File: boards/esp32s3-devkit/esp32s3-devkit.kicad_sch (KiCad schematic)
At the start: 37 parts, among them J1 Conn_01x17_Pin, J2 Conn_01x17_Pin, J3 USB_C_Receptacle_USB2.0_16P, Q1 Q_PMOS_GSD, SW1 ON/OFF, SW2 RESET, SW3 BOOT, U1 TPS630701RNMR, U2 ESP32-S3-WROOM-1, U3 USBLC6-2SC6

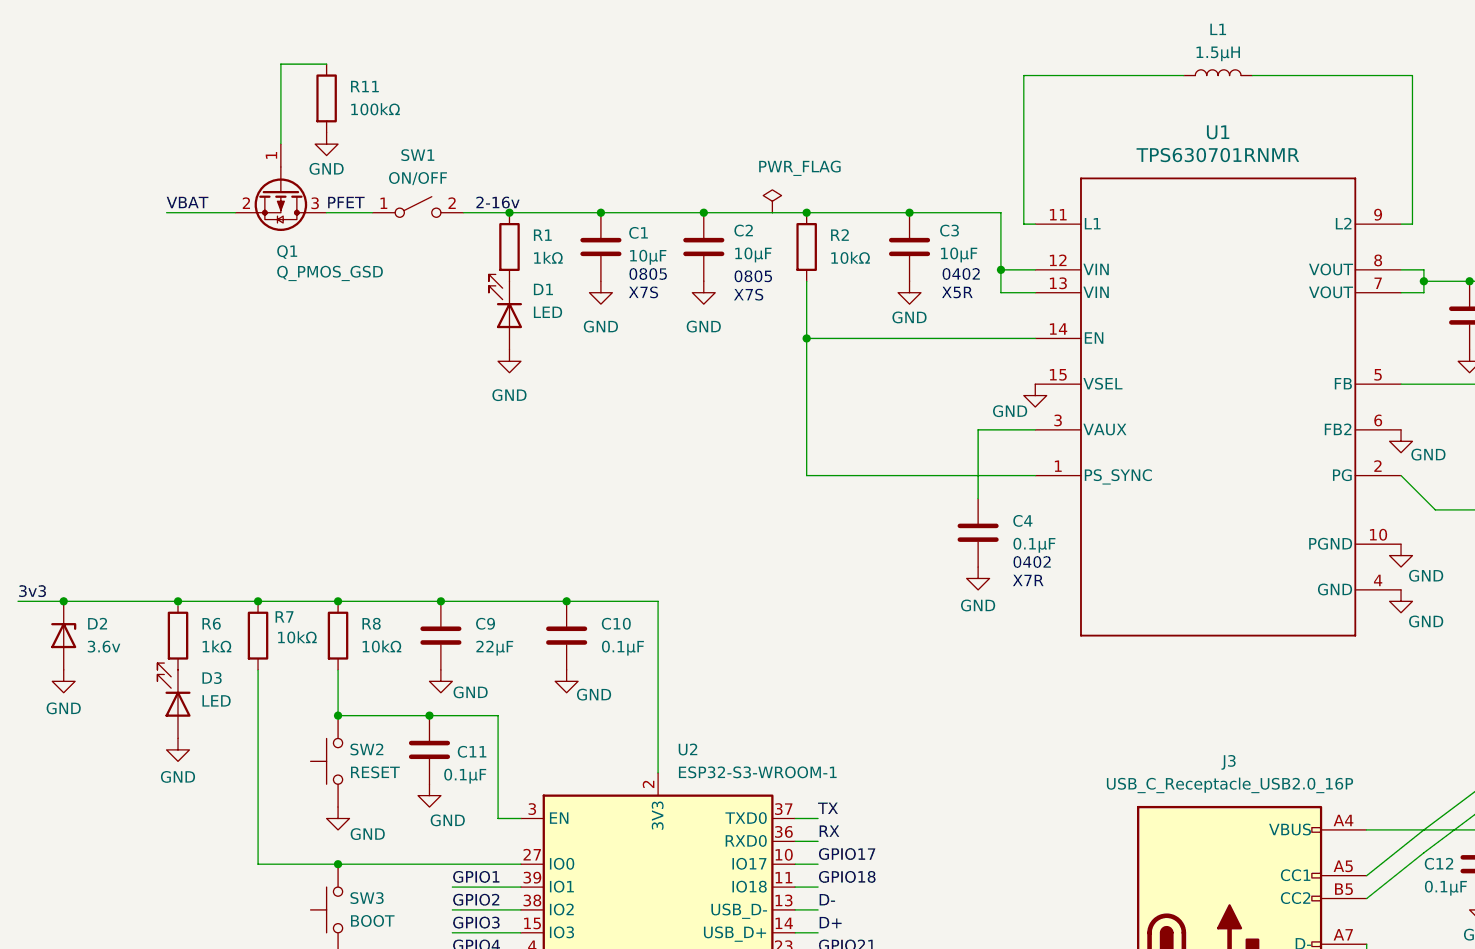
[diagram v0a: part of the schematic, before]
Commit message: fix(esp32s3-devkit): use adjustable TPS63070 instead of fixed TPS630701 (#107)
* fix(esp32s3-devkit): use adjustable TPS63070 instead of fixed TPS630701

The schematic uses a resistor divider (R3=470k, R4=150k) on the FB pin
to regulate output to 3.3V, which requires the adjustable TPS63070RNMR.
The fixed TPS630701RNMR ignores the external divider and outputs 5V.

Renames the library symbol, schematic references, and PCB value to
TPS63070RNMR throughout. Also adds JLCPCB BOM and CPL assembly files.

* fix(esp32s3-devkit): replace SW1 with MK-12C03-G015 slide switch for JLCPCB availability

The original CK RS282G05A3 SPST switch (C2804704) is out of stock at
JLCPCB. Replace with G-Switch MK-12C03-G015 SPDT slide switch
(C2890358, ~4900 in stock) using KiCad's built-in
SW_SPDT_Shouhan_MSK12C02 footprint (same package family).

Schematic changes:
- SW1 symbol changed from SW_SPST to SW_SPDT
- Pin 2 (COM) connects to /PFET, pin 1 (Throw A) to /2-16v
- Pin 3 (Throw B) marked no-connect
- Footprint updated to Button_Switch_SMD:SW_SPDT_Shouhan_MSK12C02

BOM sync with user's JLCPCB part selections:
- D1/D3: C72043 -> C2286 (red LED, in stock)
- D2: C2928910 -> C493210 (BZT52B3V6S 3.6V Zener, in stock)
- SW1: C2804704 -> C2890358 (MK-12C03-G015 slide switch)

NOTE: PCB layout update required - user must run "Update PCB from
Schematic" in KiCad, place/route the new SW1 footprint, run DRC,
and regenerate Gerber files + CPL.

* fix(esp32s3-devkit): battery-only power-path and boot-reliability fixes

- Q1 (AO3401A): correct reverse-polarity orientation - schematic
  mirrored so drain faces battery, footprint rotated 180deg so pads
  land in the correct VBAT/PFET pours, gate rerouted via B.Cu hop,
  VBAT zone corner extended to enclose the drain pad
- Rename misleading '2-16v' net to 'VBAT_SW' (board is 3xAA powered)
- C11 EN delay cap 0.1uF -> 1uF (Espressif-recommended power-on delay)
- D2 3.6V zener marked DNP (leaks near knee at 3.3V, drains battery)
- Drop pcbway-4layer-adva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
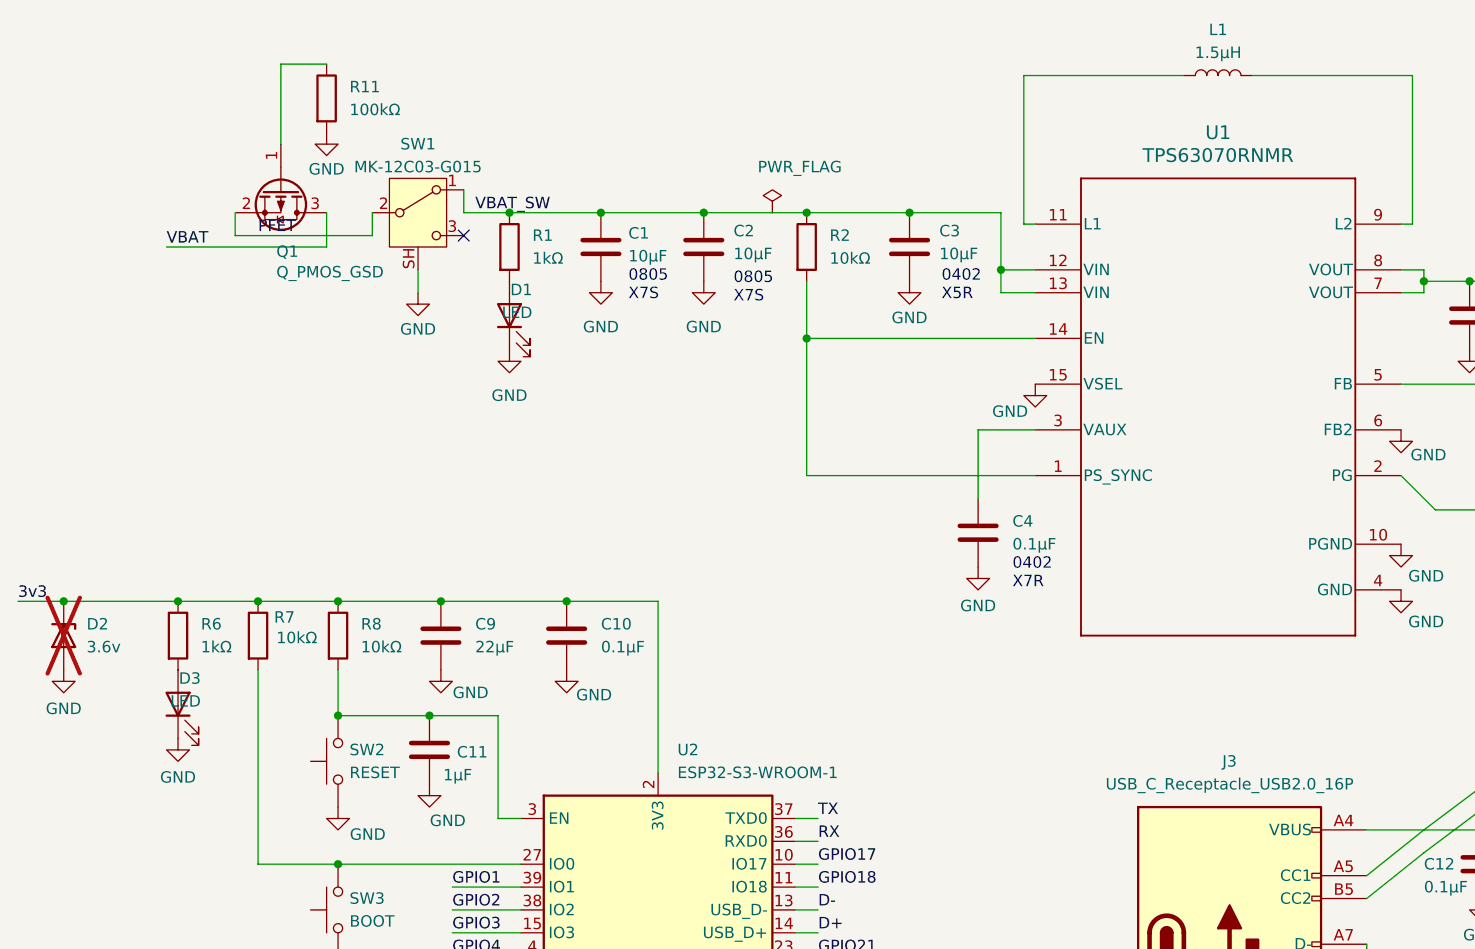
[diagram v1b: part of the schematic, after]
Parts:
- C11: value 0.1µF -> 1µF
- D2: now not fitted; now left out of the parts list
- SW1: value ON/OFF -> MK-12C03-G015; footprint Button_Switch_SMD:SW_SPST_CK_RS282G05A3 -> Button_Switch_SMD:SW_SPDT_Shouhan_MSK12C02; symbol Switch:SW_SPST -> Switch:SW_SPDT
- U1: value TPS630701RNMR -> TPS63070RNMR; symbol TPS630701 Buck-Boost:TPS630701RNMR -> TPS63070 Buck-Boost:TPS63070RNMR
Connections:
- net GND: now also D1.1 (K), D3.1 (K), SW1.SH; no longer D1.2 (A), D3.2 (A)
- net PFET: now also Q1.2 (S), SW1.2 (B); no longer Q1.3 (D), SW1.1 (A)
- net VBAT: now also Q1.3 (D); no longer Q1.2 (S)
- net at R6.2: now also D3.2 (A); no longer D3.1 (K)
- net at R1.2: now also D1.2 (A); no longer D1.1 (K)
- net 2-16v renamed VBAT_SW
- net VBAT_SW: now also SW1.1 (A); no longer SW1.2 (B)
- no-connect marks 5 -> 6
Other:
- moved on the sheet: D1, D3
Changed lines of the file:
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@@
 	)
 	(no_connect
+		(at 67.31 49.53)
+	)
+	(no_connect
 		(at 106.68 134.62)
 	)
@@
 	(wire
 		(pts
+			(xy 52.07 46.99) (xy 52.07 50.8)
+		)
+		(stroke
+			(width 0)
+			(type default)
+		)
+	)
+	(wire
+		(pts
+			(xy 52.07 50.8) (xy 34.29 50.8)
+		)
+		(stroke
+			(width 0)
+			(type default)
+		)
+	)
+	(wire
+		(pts
+			(xy 41.91 46.99) (xy 41.91 49.53)
+		)
+		(stroke
+			(width 0)
+			(type default)
+		)
+	)
+	(wire
+		(pts
+			(xy 41.91 49.53) (xy 57.15 49.53)
+		)
+		(stroke
+			(width 0)
+			(type default)
+		)
+	)
+	(wire
+		(pts
+			(xy 57.15 49.53) (xy 57.15 46.99)
+		)
+		(stroke
+			(width 0)
+			(type default)
+		)
+	)
+	(wire
+		(pts
+			(xy 62.23 53.34) (xy 62.23 55.88)
+		)
+		(stroke
+			(width 0)
+			(type default)
+		)
+	)
+	(wire
+		(pts
 			(xy 104.14 124.46) (xy 106.68 124.46)
 		)
@@
 	(wire
 		(pts
-			(xy 52.07 46.99) (xy 57.15 46.99)
-		)
-		(stroke
-			(width 0)
-			(type default)
-		)
-	)
-	(wire
-		(pts
 			(xy 187.96 120.65) (xy 187.96 127)
 		)
@@
 	(wire
 		(pts
-			(xy 184.15 110.49) (xy 190.5 110.49)
+			(xy 67.31 44.45) (xy 67.31 46.99)
 		)
 		(stroke
@@
 	(wire
 		(pts
-			(xy 104.14 152.4) (xy 106.68 152.4)
+			(xy 184.15 110.49) (xy 190.5 110.49)
 		)
 		(stroke
@@
 	(wire
 		(pts
-			(xy 34.29 46.99) (xy 41.91 46.99)
+			(xy 104.14 152.4) (xy 106.68 152.4)
 		)
 		(stroke
@@
 	)
 	(label "VBAT"
-		(at 34.29 46.99 0)
+		(at 34.29 50.8 0)
 		(effects
 			(font
@@
 	)
 	(label "PFET"
-		(at 52.07 46.99 0)
+		(at 44.45 49.53 0)
 		(effects
 			(font
@@
 		)
 	)
-	(label "2-16v"
+	(label "VBAT_SW"
 		(at 68.58 46.99 0)
 		(effects
@@
 	)
 	(symbol
+		(lib_id "power:GND")
+		(at 62.23 55.88 0)
+		(unit 1)
+		(body_style 1)
+		(exclude_from_sim no)
+		(in_bom yes)
+		(on_board yes)
+		(in_pos_files yes)
+		(dnp no)
+		(property "Reference" "#PWR030"
+			(at 62.23 62.23 0)
+			(hide yes)
+			(show_name no)
+			(do_not_autoplace no)
+			(effects
+				(font
+					(size 1.27 1.27)
+				)
+			)
+		)
+		(property "Value" "GND"
+			(at 62.23 59.944 0)
+			(show_name no)
+			(do_not_autoplace no)
+			(effects
+				(font
+					(size 1.27 1.27)
+				)
+			)
+		)
+		(property "Footprint" ""
+			(at 62.23 55.88 0)
+			(hide yes)
+			(show_name no)
+			(do_not_autoplace no)
+			(effects
+				(font
+					(size 1.27 1.27)
+				)
+			)
+		)
+		(property "Datasheet" ""
+			(at 62.23 55.88 0)
+			(hide yes)
+			(show_name no)
+			(do_not_autoplace no)
+			(effects
+				(font
+					(size 1.27 1.27)
+				)
+			)
+		)
+		(property "Description" "Power symbol creates a global label with name \"GND\" , ground"
+			(at 62.23 55.88 0)
+			(hide yes)
+			(show_name no)
+			(do_not_autoplace no)
+			(effects
+				(font
+					(size 1.27 1.27)
+				)
+			)
+		)
+		(pin "1"
+		)
+		(instances
+			(project "esp32s3-devkit"
+				(path "/7924bd8b-2498-4d76-899d-c0ad5a514485"
+					(reference "#PWR030")
+					(unit 1)
+				)
+			)
+		)
+	)
+	(symbol
 		(lib_id "Device:R")
 		(at 35.56 93.98 0)
@@
 		(body_style 1)
 		(exclude_from_sim no)
-		(in_bom yes)
+		(in_bom no)
 		(on_board yes)
 		(in_pos_files yes)
-		(dnp no)
+		(dnp yes)
 		(fields_autoplaced yes)
 		(property "Reference" "D2"
@@
 	)
 	(symbol
-		(lib_id "Switch:SW_SPST")
+		(lib_id "Switch:SW_SPDT")
 		(at 62.23 46.99 0)
 		(unit 1)
@@
 		(fields_autoplaced yes)
 		(property "Reference" "SW1"
-			(at 62.23 40.64 0)
+			(at 62.23 39.37 0)
 			(show_name no)
 			(do_not_autoplace no)
@@
 			)
 		)
-		(property "Value" "ON/OFF"
-			(at 62.23 43.18 0)
+		(property "Value" "MK-12C03-G015"
+			(at 62.23 41.91 0)
 			(show_name no)
 			(do_not_autoplace no)
@@
 			)
 		)
-		(property "Footprint" "Button_Switch_SMD:SW_SPST_CK_RS282G05A3"
+		(property "Footprint" "Button_Switch_SMD:SW_SPDT_Shouhan_MSK12C02"
 			(at 62.23 46.99 0)
 			(hide yes)
@@
 			)
 		)
-		(property "Description" "Single Pole Single Throw (SPST) switch"
+		(property "Description" "Switch, single pole double throw"
 			(at 62.23 46.99 0)
 			(hide yes)
@@
 			)
 		)
+		(pin "1"
+		)
 		(pin "2"
 		)
-		(pin "1"
+		(pin "3"
+		)
+		(pin "SH"
 		)
 		(instances
@@
 	)
 	(symbol
-		(lib_id "TPS630701 Buck-Boost:TPS630701RNMR")
+		(lib_id "TPS63070 Buck-Boost:TPS63070RNMR")
 		(at 151.13 68.58 0)
 		(unit 1)
@@
 			)
 		)
-		(property "Value" "TPS630701RNMR"
+		(property "Value" "TPS63070RNMR"
 			(at 151.13 40.64 0)
 			(show_name no)
@@
 	(symbol
 		(lib_id "Device:LED")
-		(at 35.56 101.6 270)
+		(at 35.56 101.6 90)
 		(unit 1)
 		(body_style 1)
@@
 	(symbol
 		(lib_id "Device:LED")
-		(at 72.39 58.42 270)
+		(at 72.39 58.42 90)
 		(unit 1)
 		(body_style 1)
@@
 			)
 		)
-		(property "Value" "0.1µF"
+		(property "Value" "1µF"
 			(at 65.024 109.474 0)
 			(show_name no)
